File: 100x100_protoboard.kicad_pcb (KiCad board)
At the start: 2 copper layers, 97.8 x 96.5 mm, 418 parts, among them CON1 BARREL_JACK, CON2 USB_FEMALE_WITH_ID, CON3 USB_FEMALE_WITH_ID, J1 INTERCONNECT_1X03, J10 INTERCONNECT_1X03, J11 INTERCONNECT_1X03, J12 INTERCONNECT_1X03, J13 INTERCONNECT_1X03, J14 INTERCONNECT_1X03, J15 INTERCONNECT_1X03, J16 INTERCONNECT_1X03, J17 INTERCONNECT_1X03, J18 INTERCONNECT_1X03, J19 INTERCONNECT_1X03, J2 INTERCONNECT_1X03, J20 INTERCONNECT_1X03, J21 INTERCONNECT_1X03, J22 INTERCONNECT_1X03, J23 INTERCONNECT_1X03, J24 INTERCONNECT_1X03, J25 INTERCONNECT_1X03, J26 INTERCONNECT_1X03, J27 INTERCONNECT_1X03, J28 INTERCONNECT_1X03, J29 INTERCONNECT_1X03, J3 INTERCONNECT_1X03, J30 INTERCONNECT_1X03, J31 INTERCONNECT_1X03, J32 INTERCONNECT_1X03, J33 INTERCONNECT_1X03, J34 INTERCONNECT_1X03, J35 INTERCONNECT_1X03, J36 INTERCONNECT_1X03, J37 INTERCONNECT_1X03, J38 INTERCONNECT_1X03, J39 INTERCONNECT_1X03, J4 INTERCONNECT_1X03, J40 INTERCONNECT_1X03, J41 INTERCONNECT_1X03, J42 INTERCONNECT_1X03, J43 INTERCONNECT_1X03, J44 INTERCONNECT_1X03, J45 INTERCONNECT_1X03, J46 INTERCONNECT_1X03, J47 INTERCONNECT_1X03, J48 INTERCONNECT_1X03, J49 INTERCONNECT_1X03, J5 INTERCONNECT_1X03, J50 INTERCONNECT_1X03, J51 INTERCONNECT_1X03, J52 INTERCONNECT_1X03, J53 INTERCONNECT_1X03, J54 INTERCONNECT_1X03, J55 INTERCONNECT_1X03, J56 INTERCONNECT_1X03, J57 INTERCONNECT_1X03, J58 INTERCONNECT_1X03, J59 INTERCONNECT_1X03, J6 INTERCONNECT_1X03, J60 INTERCONNECT_1X03, J61 INTERCONNECT_1X03, J62 INTERCONNECT_1X03, J63 INTERCONNECT_1X03, J64 INTERCONNECT_1X03, J65 INTERCONNECT_1X02, J7 INTERCONNECT_1X03, J8 INTERCONNECT_1X03, J9 INTERCONNECT_1X03, P1 CONN_5, P1 CONN_8X2, P2 CONN_8X2, U1 LM7805CT

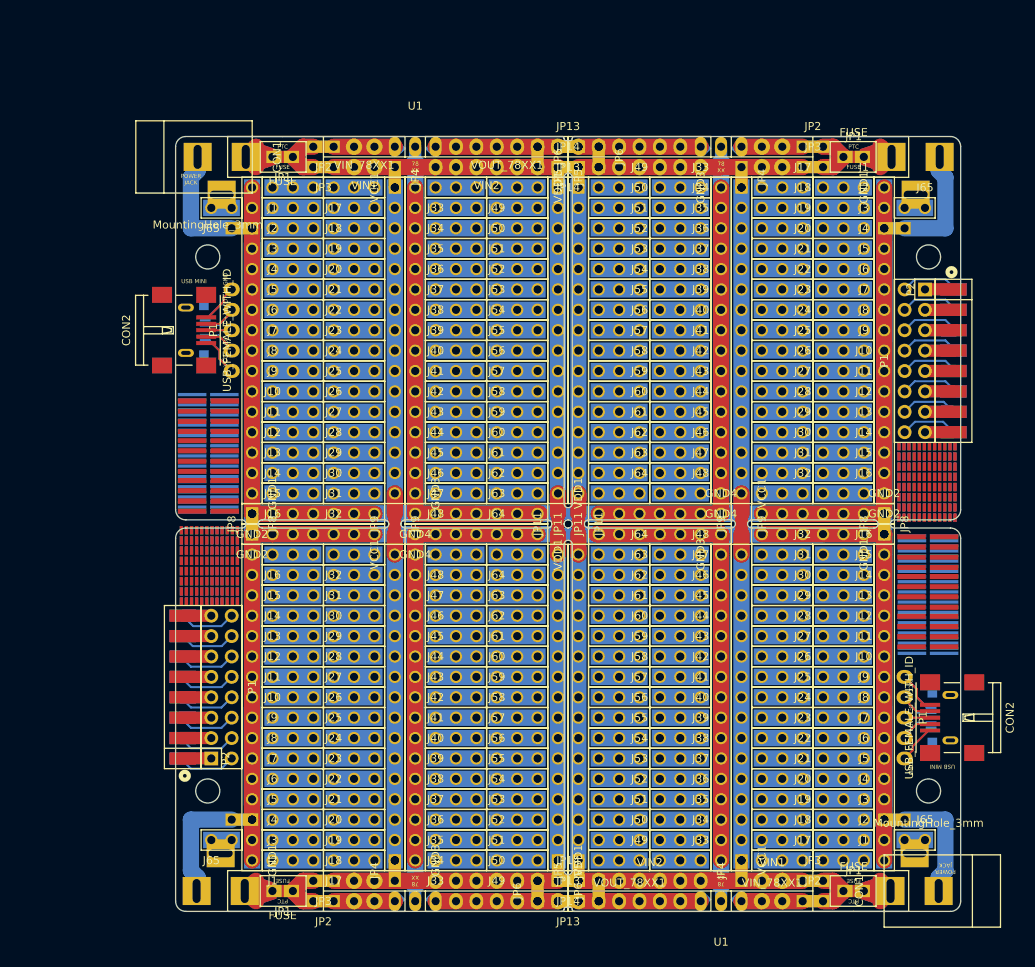
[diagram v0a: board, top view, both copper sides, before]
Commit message: remove center border outline, because drilling it plated shorts PWR and GND
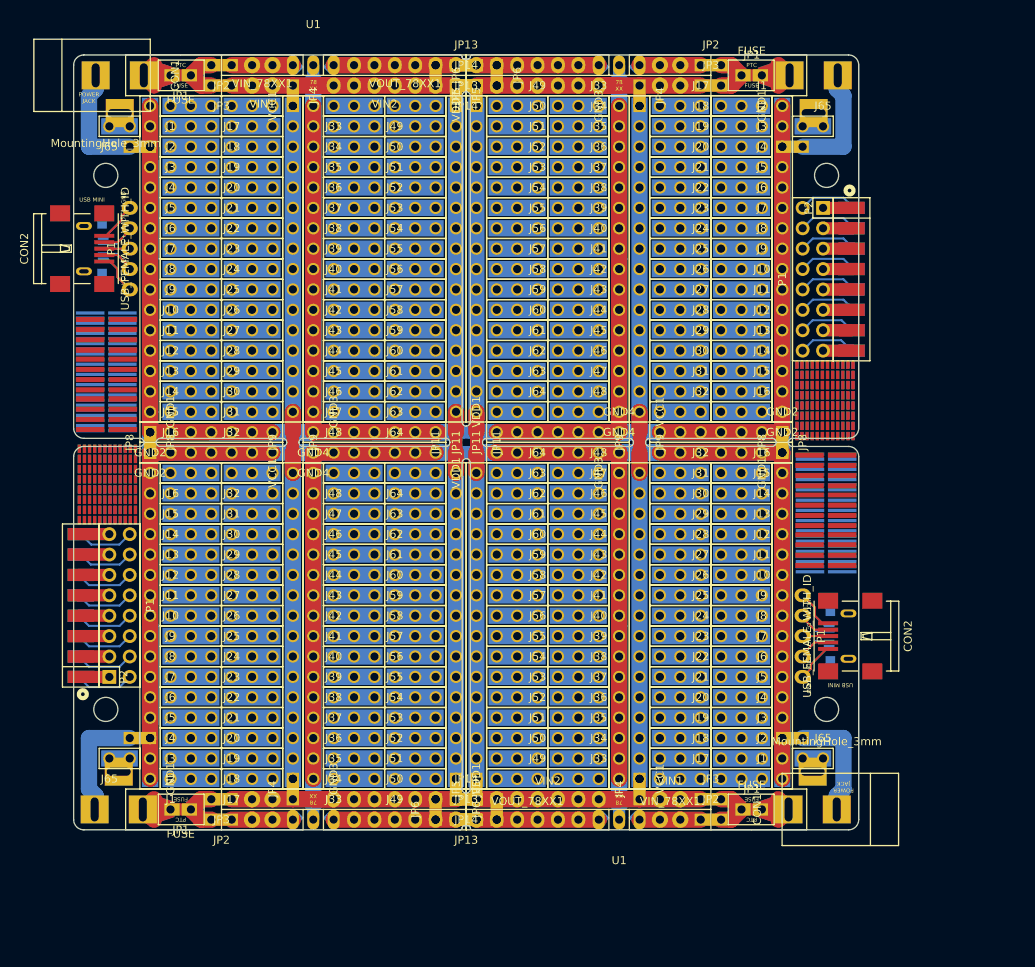
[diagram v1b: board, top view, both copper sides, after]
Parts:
- removed the C1 at (106.7, 35.3)
- removed the C1 at (106.7, 127.3)
- removed the C2 at (104.1, 35.3)
- removed the C2 at (104.1, 127.3)
- removed the CON1 at (132.8, 35.6)
- removed the CON1 at (132.7, 127.0)
- removed the F1 at (121.9, 35.6)
- removed the F1 at (121.9, 127.0)
- removed the F2 at (121.9, 35.6)
- removed the F2 at (121.9, 127.0)
- removed the GND1 at (125.7, 39.4)
- removed the GND1 at (125.7, 85.1)
- removed the GND2 at (125.7, 80.0)
- removed the GND2 at (125.7, 82.5)
- removed the GND3 at (105.4, 39.4)
- removed the GND3 at (105.4, 85.1)
- removed the GND4 at (105.4, 80.0)
- removed the GND4 at (105.4, 82.5)
- removed the J1 at (123.2, 39.4)
- removed the J1 at (123.2, 123.2)
- removed the J10 at (123.2, 62.2)
- removed the J10 at (123.2, 100.3)
- removed the J11 at (123.2, 64.8)
- removed the J11 at (123.2, 97.8)
- removed the J12 at (123.2, 67.3)
- removed the J12 at (123.2, 95.2)
- removed the J13 at (123.2, 69.8)
- removed the J13 at (123.2, 92.7)
- removed the J14 at (123.2, 72.4)
- removed the J14 at (123.2, 90.2)
- removed the J15 at (123.2, 74.9)
- removed the J15 at (123.2, 87.6)
- removed the J16 at (123.2, 77.5)
- removed the J16 at (123.2, 85.1)
- removed the J17 at (115.6, 39.4)
- removed the J17 at (115.6, 123.2)
- removed the J18 at (115.6, 41.9)
- removed the J18 at (115.6, 120.7)
- removed the J19 at (115.6, 44.5)
- removed the J19 at (115.6, 118.1)
- removed the J2 at (123.2, 41.9)
- removed the J2 at (123.2, 120.7)
- removed the J20 at (115.6, 47.0)
- removed the J20 at (115.6, 115.6)
- removed the J21 at (115.6, 49.5)
- removed the J21 at (115.6, 113.0)
- removed the J22 at (115.6, 52.1)
- removed the J22 at (115.6, 110.5)
- removed the J23 at (115.6, 54.6)
- removed the J23 at (115.6, 108.0)
- removed the J24 at (115.6, 57.1)
- removed the J24 at (115.6, 105.4)
- removed the J25 at (115.6, 59.7)
- removed the J25 at (115.6, 102.9)
- removed the J26 at (115.6, 62.2)
- removed the J26 at (115.6, 100.3)
- removed the J27 at (115.6, 64.8)
- removed the J27 at (115.6, 97.8)
- removed the J28 at (115.6, 67.3)
- removed the J28 at (115.6, 95.2)
- removed the J29 at (115.6, 69.8)
- removed the J29 at (115.6, 92.7)
- removed the J3 at (123.2, 44.5)
- removed the J3 at (123.2, 118.1)
- removed the J30 at (115.6, 72.4)
- removed the J30 at (115.6, 90.2)
- removed the J31 at (115.6, 74.9)
- removed the J31 at (115.6, 87.6)
- removed the J32 at (115.6, 77.5)
- removed the J32 at (115.6, 85.1)
- removed the J33 at (102.9, 39.4)
- removed the J33 at (102.9, 123.2)
- removed the J34 at (102.9, 41.9)
- removed the J34 at (102.9, 120.7)
- removed the J35 at (102.9, 44.5)
- removed the J35 at (102.9, 118.1)
- removed the J36 at (102.9, 47.0)
- removed the J36 at (102.9, 115.6)
- removed the J37 at (102.9, 49.5)
- removed the J37 at (102.9, 113.0)
- removed the J38 at (102.9, 52.1)
- removed the J38 at (102.9, 110.5)
- removed the J39 at (102.9, 54.6)
- removed the J39 at (102.9, 108.0)
- removed the J4 at (123.2, 47.0)
- removed the J4 at (123.2, 115.6)
- removed the J40 at (102.9, 57.1)
- removed the J40 at (102.9, 105.4)
- removed the J41 at (102.9, 59.7)
- removed the J41 at (102.9, 102.9)
- removed the J42 at (102.9, 62.2)
- removed the J42 at (102.9, 100.3)
- removed the J43 at (102.9, 64.8)
- removed the J43 at (102.9, 97.8)
- removed the J44 at (102.9, 67.3)
- removed the J44 at (102.9, 95.2)
- removed the J45 at (102.9, 69.8)
- removed the J45 at (102.9, 92.7)
- removed the J46 at (102.9, 72.4)
- removed the J46 at (102.9, 90.2)
- removed the J47 at (102.9, 74.9)
- removed the J47 at (102.9, 87.6)
- removed the J48 at (102.9, 77.5)
- removed the J48 at (102.9, 85.1)
- removed the J49 at (95.2, 39.4)
- removed the J49 at (95.2, 123.2)
- removed the J5 at (123.2, 49.5)
- removed the J5 at (123.2, 113.0)
- removed the J50 at (95.2, 41.9)
- removed the J50 at (95.2, 120.7)
- removed the J51 at (95.2, 44.5)
- removed the J51 at (95.2, 118.1)
- removed the J52 at (95.2, 47.0)
- removed the J52 at (95.2, 115.6)
- removed the J53 at (95.2, 49.5)
- removed the J53 at (95.2, 113.0)
- removed the J54 at (95.2, 52.1)
- removed the J54 at (95.2, 110.5)
- removed the J55 at (95.2, 54.6)
- removed the J55 at (95.2, 108.0)
- removed the J56 at (95.2, 57.1)
- removed the J56 at (95.2, 105.4)
- removed the J57 at (95.2, 59.7)
- removed the J57 at (95.2, 102.9)
- removed the J58 at (95.2, 62.2)
- removed the J58 at (95.2, 100.3)
- removed the J59 at (95.2, 64.8)
- removed the J59 at (95.2, 97.8)
- removed the J6 at (123.2, 52.1)
- removed the J6 at (123.2, 110.5)
- removed the J60 at (95.2, 67.3)
- removed the J60 at (95.2, 95.2)
- removed the J61 at (95.2, 69.8)
- removed the J61 at (95.2, 92.7)
- removed the J62 at (95.2, 72.4)
- removed the J62 at (95.2, 90.2)
- removed the J63 at (95.2, 74.9)
- removed the J63 at (95.2, 87.6)
- removed the J64 at (95.2, 77.5)
- removed the J64 at (95.2, 85.1)
- removed the J65 at (130.8, 41.9)
- removed the J65 at (130.8, 120.7)
- removed the J7 at (123.2, 54.6)
- removed the J7 at (123.2, 108.0)
- removed the J8 at (123.2, 57.1)
- removed the J8 at (123.2, 105.4)
- removed the J9 at (123.2, 59.7)
- removed the J9 at (123.2, 102.9)
- removed the JP1 at (121.9, 35.6)
- removed the JP1 at (121.9, 127.0)
- removed the JP10 at (87.6, 81.3) (x2)
- removed the JP11 at (87.6, 81.3) (x2)
- removed the JP12 at (86.4, 80.0)
- removed the JP12 at (86.4, 82.5)
- removed the JP13 at (86.4, 34.3)
- removed the JP13 at (86.4, 128.3)
- removed the JP14 at (86.4, 36.8)
- removed the JP14 at (86.4, 125.7)
- removed the JP15 at (108.0, 81.3) (x2)
- removed the JP2 at (116.8, 34.3)
- removed the JP2 at (116.8, 128.3)
- removed the JP3 at (116.8, 36.8)
- removed the JP3 at (116.8, 125.7)
- removed the JP4 at (108.0, 38.1)
- removed the JP4 at (108.0, 124.5)
- removed the JP5 at (87.6, 38.1)
- removed the JP5 at (87.6, 124.5)
- removed the JP6 at (90.2, 35.6)
- removed the JP6 at (90.2, 127.0)
- removed the JP7 at (127.0, 44.5)
- removed the JP7 at (127.0, 118.1)
- removed the JP8 at (125.7, 81.3) (x2)
- removed the JP9 at (108.0, 81.3) (x2)
- removed the MountingHole_3mm at (131.2, 48.0)
- removed the MountingHole_3mm at (131.2, 114.5)
- removed the P1 at (129.5, 61.0)
- removed the P1 at (128.3, 105.4)
- removed the Ref** at (131.7, 78.6) (x2)
- removed the Ref** at (131.2, 95.2)
- removed the Ref** at (131.7, 73.5) (x2)
- removed the Ref** at (131.2, 94.7)
- removed the Ref** at (131.2, 89.7)
- removed the Ref** at (131.2, 84.8)
- removed the Ref** at (131.2, 85.0)
- removed the Ref** at (131.2, 90.1)
- removed the U1 at (105.4, 34.3)
- removed the U1 at (105.4, 128.3)
- removed the VCC1 at (108.0, 77.5)
- removed the VCC1 at (108.0, 123.2)
- removed the VDD1 at (87.6, 39.4)
- removed the VDD1 at (87.6, 85.1)
- removed the VIN1 at (111.8, 36.8)
- removed the VIN1 at (111.8, 125.7)
- removed the VIN2 at (96.5, 36.8)
- removed the VIN2 at (96.5, 125.7)
- removed the VIN_78XX1 at (111.8, 34.3)
- removed the VIN_78XX1 at (111.8, 128.3)
- removed the VOUT_78XX1 at (94.0, 34.3)
- removed the VOUT_78XX1 at (94.0, 128.3)
- added C1: u33, Capacitors_SMD:C_0805_HandSoldering, B.Cu at (94.0, 25.1)
- added C1: u33, Capacitors_SMD:C_0805_HandSoldering, B.Cu at (94.0, 117.1)
- added C2: u1, Capacitors_SMD:C_0805_HandSoldering, B.Cu at (91.4, 25.1)
- added C2: u1, Capacitors_SMD:C_0805_HandSoldering, B.Cu at (91.4, 117.1)
- added CON1: BARREL_JACK, Connect:BARREL_JACK, B.Cu at (120.1, 25.4)
- added CON1: BARREL_JACK, Connect:BARREL_JACK, F.Cu at (120.0, 116.8)
- added F1: FUSE, Muonde:CC12ZZ, B.Cu at (109.2, 25.4)
- added F1: FUSE, Muonde:CC12ZZ, F.Cu at (109.2, 116.8)
- added F2: FUSE, Muonde:CC12ZZ, F.Cu at (109.2, 25.4)
- added F2: FUSE, Muonde:CC12ZZ, B.Cu at (109.2, 116.8)
- added GND1: INTERCONNECT_1X16, 2.54mm_Pin_Headers:Interconnect_1x16, F.Cu at (113.0, 29.2)
- added GND1: INTERCONNECT_1X16, 2.54mm_Pin_Headers:Interconnect_1x16, F.Cu at (113.0, 74.9)
- added GND2: INTERCONNECT_1X07, 2.54mm_Pin_Headers:Interconnect_1x07, F.Cu at (113.0, 69.8)
- added GND2: INTERCONNECT_1X07, 2.54mm_Pin_Headers:Interconnect_1x07, F.Cu at (113.0, 72.4)
- added GND3: INTERCONNECT_1X16, 2.54mm_Pin_Headers:Interconnect_1x16, F.Cu at (92.7, 29.2)
- added GND3: INTERCONNECT_1X16, 2.54mm_Pin_Headers:Interconnect_1x16, F.Cu at (92.7, 74.9)
- added GND4: INTERCONNECT_1X07, 2.54mm_Pin_Headers:Interconnect_1x07, F.Cu at (92.7, 69.8)
- added GND4: INTERCONNECT_1X07, 2.54mm_Pin_Headers:Interconnect_1x07, F.Cu at (92.7, 72.4)
- added J1: INTERCONNECT_1X03, 2.54mm_Pin_Headers:Interconnect_1x03, F.Cu at (110.5, 29.2)
- added J1: INTERCONNECT_1X03, 2.54mm_Pin_Headers:Interconnect_1x03, F.Cu at (110.5, 113.0)
- added J10: INTERCONNECT_1X03, 2.54mm_Pin_Headers:Interconnect_1x03, F.Cu at (110.5, 52.1)
- added J10: INTERCONNECT_1X03, 2.54mm_Pin_Headers:Interconnect_1x03, F.Cu at (110.5, 90.2)
- added J11: INTERCONNECT_1X03, 2.54mm_Pin_Headers:Interconnect_1x03, F.Cu at (110.5, 54.6)
- added J11: INTERCONNECT_1X03, 2.54mm_Pin_Headers:Interconnect_1x03, F.Cu at (110.5, 87.6)
- added J12: INTERCONNECT_1X03, 2.54mm_Pin_Headers:Interconnect_1x03, F.Cu at (110.5, 57.1)
- added J12: INTERCONNECT_1X03, 2.54mm_Pin_Headers:Interconnect_1x03, F.Cu at (110.5, 85.1)
- added J13: INTERCONNECT_1X03, 2.54mm_Pin_Headers:Interconnect_1x03, F.Cu at (110.5, 59.7)
- added J13: INTERCONNECT_1X03, 2.54mm_Pin_Headers:Interconnect_1x03, F.Cu at (110.5, 82.5)
- added J14: INTERCONNECT_1X03, 2.54mm_Pin_Headers:Interconnect_1x03, F.Cu at (110.5, 62.2)
- added J14: INTERCONNECT_1X03, 2.54mm_Pin_Headers:Interconnect_1x03, F.Cu at (110.5, 80.0)
- added J15: INTERCONNECT_1X03, 2.54mm_Pin_Headers:Interconnect_1x03, F.Cu at (110.5, 64.8)
- added J15: INTERCONNECT_1X03, 2.54mm_Pin_Headers:Interconnect_1x03, F.Cu at (110.5, 77.5)
- added J16: INTERCONNECT_1X03, 2.54mm_Pin_Headers:Interconnect_1x03, F.Cu at (110.5, 67.3)
- added J16: INTERCONNECT_1X03, 2.54mm_Pin_Headers:Interconnect_1x03, F.Cu at (110.5, 74.9)
- added J17: INTERCONNECT_1X03, 2.54mm_Pin_Headers:Interconnect_1x03, F.Cu at (102.9, 29.2)
- added J17: INTERCONNECT_1X03, 2.54mm_Pin_Headers:Interconnect_1x03, F.Cu at (102.9, 113.0)
- added J18: INTERCONNECT_1X03, 2.54mm_Pin_Headers:Interconnect_1x03, F.Cu at (102.9, 31.8)
- added J18: INTERCONNECT_1X03, 2.54mm_Pin_Headers:Interconnect_1x03, F.Cu at (102.9, 110.5)
- added J19: INTERCONNECT_1X03, 2.54mm_Pin_Headers:Interconnect_1x03, F.Cu at (102.9, 34.3)
- added J19: INTERCONNECT_1X03, 2.54mm_Pin_Headers:Interconnect_1x03, F.Cu at (102.9, 108.0)
- added J2: INTERCONNECT_1X03, 2.54mm_Pin_Headers:Interconnect_1x03, F.Cu at (110.5, 31.8)
- added J2: INTERCONNECT_1X03, 2.54mm_Pin_Headers:Interconnect_1x03, F.Cu at (110.5, 110.5)
- added J20: INTERCONNECT_1X03, 2.54mm_Pin_Headers:Interconnect_1x03, F.Cu at (102.9, 36.8)
- added J20: INTERCONNECT_1X03, 2.54mm_Pin_Headers:Interconnect_1x03, F.Cu at (102.9, 105.4)
- added J21: INTERCONNECT_1X03, 2.54mm_Pin_Headers:Interconnect_1x03, F.Cu at (102.9, 39.4)
- added J21: INTERCONNECT_1X03, 2.54mm_Pin_Headers:Interconnect_1x03, F.Cu at (102.9, 102.9)
- added J22: INTERCONNECT_1X03, 2.54mm_Pin_Headers:Interconnect_1x03, F.Cu at (102.9, 41.9)
- added J22: INTERCONNECT_1X03, 2.54mm_Pin_Headers:Interconnect_1x03, F.Cu at (102.9, 100.3)
- added J23: INTERCONNECT_1X03, 2.54mm_Pin_Headers:Interconnect_1x03, F.Cu at (102.9, 44.5)
- added J23: INTERCONNECT_1X03, 2.54mm_Pin_Headers:Interconnect_1x03, F.Cu at (102.9, 97.8)
- added J24: INTERCONNECT_1X03, 2.54mm_Pin_Headers:Interconnect_1x03, F.Cu at (102.9, 47.0)
- added J24: INTERCONNECT_1X03, 2.54mm_Pin_Headers:Interconnect_1x03, F.Cu at (102.9, 95.2)
- added J25: INTERCONNECT_1X03, 2.54mm_Pin_Headers:Interconnect_1x03, F.Cu at (102.9, 49.5)
- added J25: INTERCONNECT_1X03, 2.54mm_Pin_Headers:Interconnect_1x03, F.Cu at (102.9, 92.7)
- added J26: INTERCONNECT_1X03, 2.54mm_Pin_Headers:Interconnect_1x03, F.Cu at (102.9, 52.1)
- added J26: INTERCONNECT_1X03, 2.54mm_Pin_Headers:Interconnect_1x03, F.Cu at (102.9, 90.2)
- added J27: INTERCONNECT_1X03, 2.54mm_Pin_Headers:Interconnect_1x03, F.Cu at (102.9, 54.6)
- added J27: INTERCONNECT_1X03, 2.54mm_Pin_Headers:Interconnect_1x03, F.Cu at (102.9, 87.6)
- added J28: INTERCONNECT_1X03, 2.54mm_Pin_Headers:Interconnect_1x03, F.Cu at (102.9, 57.1)
- added J28: INTERCONNECT_1X03, 2.54mm_Pin_Headers:Interconnect_1x03, F.Cu at (102.9, 85.1)
- added J29: INTERCONNECT_1X03, 2.54mm_Pin_Headers:Interconnect_1x03, F.Cu at (102.9, 59.7)
- added J29: INTERCONNECT_1X03, 2.54mm_Pin_Headers:Interconnect_1x03, F.Cu at (102.9, 82.5)
- added J3: INTERCONNECT_1X03, 2.54mm_Pin_Headers:Interconnect_1x03, F.Cu at (110.5, 34.3)
- added J3: INTERCONNECT_1X03, 2.54mm_Pin_Headers:Interconnect_1x03, F.Cu at (110.5, 108.0)
- added J30: INTERCONNECT_1X03, 2.54mm_Pin_Headers:Interconnect_1x03, F.Cu at (102.9, 62.2)
- added J30: INTERCONNECT_1X03, 2.54mm_Pin_Headers:Interconnect_1x03, F.Cu at (102.9, 80.0)
- added J31: INTERCONNECT_1X03, 2.54mm_Pin_Headers:Interconnect_1x03, F.Cu at (102.9, 64.8)
- added J31: INTERCONNECT_1X03, 2.54mm_Pin_Headers:Interconnect_1x03, F.Cu at (102.9, 77.5)
- added J32: INTERCONNECT_1X03, 2.54mm_Pin_Headers:Interconnect_1x03, F.Cu at (102.9, 67.3)
- added J32: INTERCONNECT_1X03, 2.54mm_Pin_Headers:Interconnect_1x03, F.Cu at (102.9, 74.9)
- added J33: INTERCONNECT_1X03, 2.54mm_Pin_Headers:Interconnect_1x03, F.Cu at (90.2, 29.2)
- added J33: INTERCONNECT_1X03, 2.54mm_Pin_Headers:Interconnect_1x03, F.Cu at (90.2, 113.0)
- added J34: INTERCONNECT_1X03, 2.54mm_Pin_Headers:Interconnect_1x03, F.Cu at (90.2, 31.8)
- added J34: INTERCONNECT_1X03, 2.54mm_Pin_Headers:Interconnect_1x03, F.Cu at (90.2, 110.5)
- added J35: INTERCONNECT_1X03, 2.54mm_Pin_Headers:Interconnect_1x03, F.Cu at (90.2, 34.3)
- added J35: INTERCONNECT_1X03, 2.54mm_Pin_Headers:Interconnect_1x03, F.Cu at (90.2, 108.0)
- added J36: INTERCONNECT_1X03, 2.54mm_Pin_Headers:Interconnect_1x03, F.Cu at (90.2, 36.8)
- added J36: INTERCONNECT_1X03, 2.54mm_Pin_Headers:Interconnect_1x03, F.Cu at (90.2, 105.4)
- added J37: INTERCONNECT_1X03, 2.54mm_Pin_Headers:Interconnect_1x03, F.Cu at (90.2, 39.4)
- added J37: INTERCONNECT_1X03, 2.54mm_Pin_Headers:Interconnect_1x03, F.Cu at (90.2, 102.9)
- added J38: INTERCONNECT_1X03, 2.54mm_Pin_Headers:Interconnect_1x03, F.Cu at (90.2, 41.9)
- added J38: INTERCONNECT_1X03, 2.54mm_Pin_Headers:Interconnect_1x03, F.Cu at (90.2, 100.3)
- added J39: INTERCONNECT_1X03, 2.54mm_Pin_Headers:Interconnect_1x03, F.Cu at (90.2, 44.5)
- added J39: INTERCONNECT_1X03, 2.54mm_Pin_Headers:Interconnect_1x03, F.Cu at (90.2, 97.8)
- added J4: INTERCONNECT_1X03, 2.54mm_Pin_Headers:Interconnect_1x03, F.Cu at (110.5, 36.8)
- added J4: INTERCONNECT_1X03, 2.54mm_Pin_Headers:Interconnect_1x03, F.Cu at (110.5, 105.4)
- added J40: INTERCONNECT_1X03, 2.54mm_Pin_Headers:Interconnect_1x03, F.Cu at (90.2, 47.0)
- added J40: INTERCONNECT_1X03, 2.54mm_Pin_Headers:Interconnect_1x03, F.Cu at (90.2, 95.2)
- added J41: INTERCONNECT_1X03, 2.54mm_Pin_Headers:Interconnect_1x03, F.Cu at (90.2, 49.5)
- added J41: INTERCONNECT_1X03, 2.54mm_Pin_Headers:Interconnect_1x03, F.Cu at (90.2, 92.7)
- added J42: INTERCONNECT_1X03, 2.54mm_Pin_Headers:Interconnect_1x03, F.Cu at (90.2, 52.1)
- added J42: INTERCONNECT_1X03, 2.54mm_Pin_Headers:Interconnect_1x03, F.Cu at (90.2, 90.2)
- added J43: INTERCONNECT_1X03, 2.54mm_Pin_Headers:Interconnect_1x03, F.Cu at (90.2, 54.6)
- added J43: INTERCONNECT_1X03, 2.54mm_Pin_Headers:Interconnect_1x03, F.Cu at (90.2, 87.6)
- added J44: INTERCONNECT_1X03, 2.54mm_Pin_Headers:Interconnect_1x03, F.Cu at (90.2, 57.1)
- added J44: INTERCONNECT_1X03, 2.54mm_Pin_Headers:Interconnect_1x03, F.Cu at (90.2, 85.1)
- added J45: INTERCONNECT_1X03, 2.54mm_Pin_Headers:Interconnect_1x03, F.Cu at (90.2, 59.7)
- added J45: INTERCONNECT_1X03, 2.54mm_Pin_Headers:Interconnect_1x03, F.Cu at (90.2, 82.5)
- added J46: INTERCONNECT_1X03, 2.54mm_Pin_Headers:Interconnect_1x03, F.Cu at (90.2, 62.2)
- added J46: INTERCONNECT_1X03, 2.54mm_Pin_Headers:Interconnect_1x03, F.Cu at (90.2, 80.0)
- added J47: INTERCONNECT_1X03, 2.54mm_Pin_Headers:Interconnect_1x03, F.Cu at (90.2, 64.8)
- added J47: INTERCONNECT_1X03, 2.54mm_Pin_Headers:Interconnect_1x03, F.Cu at (90.2, 77.5)
- added J48: INTERCONNECT_1X03, 2.54mm_Pin_Headers:Interconnect_1x03, F.Cu at (90.2, 67.3)
- added J48: INTERCONNECT_1X03, 2.54mm_Pin_Headers:Interconnect_1x03, F.Cu at (90.2, 74.9)
- added J49: INTERCONNECT_1X03, 2.54mm_Pin_Headers:Interconnect_1x03, F.Cu at (82.5, 29.2)
- added J49: INTERCONNECT_1X03, 2.54mm_Pin_Headers:Interconnect_1x03, F.Cu at (82.5, 113.0)
- added J5: INTERCONNECT_1X03, 2.54mm_Pin_Headers:Interconnect_1x03, F.Cu at (110.5, 39.4)
- added J5: INTERCONNECT_1X03, 2.54mm_Pin_Headers:Interconnect_1x03, F.Cu at (110.5, 102.9)
- added J50: INTERCONNECT_1X03, 2.54mm_Pin_Headers:Interconnect_1x03, F.Cu at (82.5, 31.8)
- added J50: INTERCONNECT_1X03, 2.54mm_Pin_Headers:Interconnect_1x03, F.Cu at (82.5, 110.5)
- added J51: INTERCONNECT_1X03, 2.54mm_Pin_Headers:Interconnect_1x03, F.Cu at (82.5, 34.3)
- added J51: INTERCONNECT_1X03, 2.54mm_Pin_Headers:Interconnect_1x03, F.Cu at (82.5, 108.0)
- added J52: INTERCONNECT_1X03, 2.54mm_Pin_Headers:Interconnect_1x03, F.Cu at (82.5, 36.8)
- added J52: INTERCONNECT_1X03, 2.54mm_Pin_Headers:Interconnect_1x03, F.Cu at (82.5, 105.4)
- added J53: INTERCONNECT_1X03, 2.54mm_Pin_Headers:Interconnect_1x03, F.Cu at (82.5, 39.4)
- added J53: INTERCONNECT_1X03, 2.54mm_Pin_Headers:Interconnect_1x03, F.Cu at (82.5, 102.9)
- added J54: INTERCONNECT_1X03, 2.54mm_Pin_Headers:Interconnect_1x03, F.Cu at (82.5, 41.9)
- added J54: INTERCONNECT_1X03, 2.54mm_Pin_Headers:Interconnect_1x03, F.Cu at (82.5, 100.3)
- added J55: INTERCONNECT_1X03, 2.54mm_Pin_Headers:Interconnect_1x03, F.Cu at (82.5, 44.5)
- added J55: INTERCONNECT_1X03, 2.54mm_Pin_Headers:Interconnect_1x03, F.Cu at (82.5, 97.8)
- added J56: INTERCONNECT_1X03, 2.54mm_Pin_Headers:Interconnect_1x03, F.Cu at (82.5, 47.0)
- added J56: INTERCONNECT_1X03, 2.54mm_Pin_Headers:Interconnect_1x03, F.Cu at (82.5, 95.2)
- added J57: INTERCONNECT_1X03, 2.54mm_Pin_Headers:Interconnect_1x03, F.Cu at (82.5, 49.5)
- added J57: INTERCONNECT_1X03, 2.54mm_Pin_Headers:Interconnect_1x03, F.Cu at (82.5, 92.7)
- added J58: INTERCONNECT_1X03, 2.54mm_Pin_Headers:Interconnect_1x03, F.Cu at (82.5, 52.1)
- added J58: INTERCONNECT_1X03, 2.54mm_Pin_Headers:Interconnect_1x03, F.Cu at (82.5, 90.2)
- added J59: INTERCONNECT_1X03, 2.54mm_Pin_Headers:Interconnect_1x03, F.Cu at (82.5, 54.6)
- added J59: INTERCONNECT_1X03, 2.54mm_Pin_Headers:Interconnect_1x03, F.Cu at (82.5, 87.6)
- added J6: INTERCONNECT_1X03, 2.54mm_Pin_Headers:Interconnect_1x03, F.Cu at (110.5, 41.9)
- added J6: INTERCONNECT_1X03, 2.54mm_Pin_Headers:Interconnect_1x03, F.Cu at (110.5, 100.3)
- added J60: INTERCONNECT_1X03, 2.54mm_Pin_Headers:Interconnect_1x03, F.Cu at (82.5, 57.1)
- added J60: INTERCONNECT_1X03, 2.54mm_Pin_Headers:Interconnect_1x03, F.Cu at (82.5, 85.1)
- added J61: INTERCONNECT_1X03, 2.54mm_Pin_Headers:Interconnect_1x03, F.Cu at (82.5, 59.7)
- added J61: INTERCONNECT_1X03, 2.54mm_Pin_Headers:Interconnect_1x03, F.Cu at (82.5, 82.5)
- added J62: INTERCONNECT_1X03, 2.54mm_Pin_Headers:Interconnect_1x03, F.Cu at (82.5, 62.2)
- added J62: INTERCONNECT_1X03, 2.54mm_Pin_Headers:Interconnect_1x03, F.Cu at (82.5, 80.0)
- added J63: INTERCONNECT_1X03, 2.54mm_Pin_Headers:Interconnect_1x03, F.Cu at (82.5, 64.8)
- added J63: INTERCONNECT_1X03, 2.54mm_Pin_Headers:Interconnect_1x03, F.Cu at (82.5, 77.5)
- added J64: INTERCONNECT_1X03, 2.54mm_Pin_Headers:Interconnect_1x03, F.Cu at (82.5, 67.3)
- added J64: INTERCONNECT_1X03, 2.54mm_Pin_Headers:Interconnect_1x03, F.Cu at (82.5, 74.9)
- added J65: INTERCONNECT_1X02, 2.54mm_Pin_Headers:Interconnect_1x02, F.Cu at (118.1, 31.8)
- added J65: INTERCONNECT_1X02, 2.54mm_Pin_Headers:Interconnect_1x02, F.Cu at (118.1, 110.5)
- added J7: INTERCONNECT_1X03, 2.54mm_Pin_Headers:Interconnect_1x03, F.Cu at (110.5, 44.5)
- added J7: INTERCONNECT_1X03, 2.54mm_Pin_Headers:Interconnect_1x03, F.Cu at (110.5, 97.8)
- added J8: INTERCONNECT_1X03, 2.54mm_Pin_Headers:Interconnect_1x03, F.Cu at (110.5, 47.0)
- added J8: INTERCONNECT_1X03, 2.54mm_Pin_Headers:Interconnect_1x03, F.Cu at (110.5, 95.2)
- added J9: INTERCONNECT_1X03, 2.54mm_Pin_Headers:Interconnect_1x03, F.Cu at (110.5, 49.5)
- added J9: INTERCONNECT_1X03, 2.54mm_Pin_Headers:Interconnect_1x03, F.Cu at (110.5, 92.7)
- added JP1: JUMPER, 2.54mm_Pin_Headers:Solder_Jumper_1x2_Shorted_T, F.Cu at (109.2, 25.4)
- added JP1: JUMPER, 2.54mm_Pin_Headers:Solder_Jumper_1x2_Shorted_T, F.Cu at (109.2, 116.8)
- added JP10 (x2): JUMPER, 2.54mm_Pin_Headers:Solder_Jumper_SMD_1x2_Shorted, B.Cu at (74.9, 71.1)
- added JP11 (x2): JUMPER, 2.54mm_Pin_Headers:Solder_Jumper_SMD_1x2_Shorted, F.Cu at (74.9, 71.1)
- added JP12: JUMPER, 2.54mm_Pin_Headers:Solder_Jumper_SMD_1x2_Shorted, B.Cu at (73.7, 69.8)
- added JP12: JUMPER, 2.54mm_Pin_Headers:Solder_Jumper_SMD_1x2_Shorted, B.Cu at (73.7, 72.4)
- added JP13: JUMPER, 2.54mm_Pin_Headers:Solder_Jumper_1x2_Shorted_T, F.Cu at (73.7, 24.1)
- added JP13: JUMPER, 2.54mm_Pin_Headers:Solder_Jumper_1x2_Shorted_T, F.Cu at (73.7, 118.1)
- added JP14: JUMPER, 2.54mm_Pin_Headers:Solder_Jumper_1x2_Shorted_T, F.Cu at (73.7, 26.7)
- added JP14: JUMPER, 2.54mm_Pin_Headers:Solder_Jumper_1x2_Shorted_T, F.Cu at (73.7, 115.6)
- added JP15 (x2): JUMPER, 2.54mm_Pin_Headers:Solder_Jumper_SMD_1x2, B.Cu at (95.2, 71.1)
- added JP2: JUMPER, 2.54mm_Pin_Headers:Solder_Jumper_1x2_Shorted_T, F.Cu at (104.1, 24.1)
- added JP2: JUMPER, 2.54mm_Pin_Headers:Solder_Jumper_1x2_Shorted_T, F.Cu at (104.1, 118.1)
- added JP3: JUMPER, 2.54mm_Pin_Headers:Solder_Jumper_1x2_Shorted_T, F.Cu at (104.1, 26.7)
- added JP3: JUMPER, 2.54mm_Pin_Headers:Solder_Jumper_1x2_Shorted_T, F.Cu at (104.1, 115.6)
- added JP4: JUMPER, 2.54mm_Pin_Headers:Solder_Jumper_1x2_Shorted_T, F.Cu at (95.2, 27.9)
- added JP4: JUMPER, 2.54mm_Pin_Headers:Solder_Jumper_1x2_Shorted_T, F.Cu at (95.2, 114.3)
- added JP5: JUMPER, 2.54mm_Pin_Headers:Solder_Jumper_1x2_Shorted_T, F.Cu at (74.9, 27.9)
- added JP5: JUMPER, 2.54mm_Pin_Headers:Solder_Jumper_1x2_Shorted_T, F.Cu at (74.9, 114.3)
- added JP6: JUMPER, 2.54mm_Pin_Headers:Solder_Jumper_1x2_Shorted_T, F.Cu at (77.5, 25.4)
- added JP6: JUMPER, 2.54mm_Pin_Headers:Solder_Jumper_1x2_Shorted_T, F.Cu at (77.5, 116.8)
- added JP7: JUMPER, 2.54mm_Pin_Headers:Solder_Jumper_1x2_Shorted_T, B.Cu at (114.3, 34.3)
- added JP7: JUMPER, 2.54mm_Pin_Headers:Solder_Jumper_1x2_Shorted_T, B.Cu at (114.3, 108.0)
- added JP8 (x2): JUMPER, 2.54mm_Pin_Headers:Solder_Jumper_1x2, F.Cu at (113.0, 71.1)
- added JP9 (x2): JUMPER, 2.54mm_Pin_Headers:Solder_Jumper_SMD_1x2_Shorted, F.Cu at (95.2, 71.1)
- added MountingHole_3mm: VAL**, Mounting_Holes:MountingHole_3mm, B.Cu at (118.5, 37.9)
- added MountingHole_3mm: VAL**, Mounting_Holes:MountingHole_3mm, F.Cu at (118.5, 104.4)
- added P1: CONN_8X2, Socket_Strips:Socket_Strip_Straight_2x08, F.Cu at (116.8, 50.8)
- added P1: CONN_5, Socket_Strips:Socket_Strip_Straight_1x05, F.Cu at (115.6, 95.2)
- added Ref**: Val**, SMD:SMD_127_065_grid_4X12, F.Cu at (119.0, 68.4)
- added Ref**: Val**, SMD:SMD_065_357_8X2, B.Cu at (118.5, 85.0)
- added Ref**: Val**, SMD:SMD_127_065_grid_4X12, F.Cu at (119.0, 63.3)
- added Ref**: Val**, SMD:SMD_127_065_grid_4X12, B.Cu at (119.0, 68.4)
- added Ref**: Val**, SMD:SMD_127_065_grid_4X12, B.Cu at (119.0, 63.3)
- added Ref**: Val**, SMD:SMD_127_357_4X2, F.Cu at (118.5, 84.5)
- added Ref**: Val**, SMD:SMD_127_357_4X2, F.Cu at (118.5, 79.6)
- added Ref**: Val**, SMD:SMD_127_357_4X2, F.Cu at (118.5, 74.6)
- added Ref**: Val**, SMD:SMD_065_357_8X2, B.Cu at (118.5, 74.8)
- added Ref**: Val**, SMD:SMD_065_357_8X2, B.Cu at (118.5, 79.9)
- added U1: LM7805CT, Transistors_TO-220:TO-220_Neutral123_Vertical, B.Cu at (92.7, 24.1)
- added U1: LM7805CT, Transistors_TO-220:TO-220_Neutral123_Vertical, F.Cu at (92.7, 118.1)
- added VCC1: INTERCONNECT_1X16, 2.54mm_Pin_Headers:Interconnect_1x16, F.Cu at (95.2, 67.3)
- added VCC1: INTERCONNECT_1X16, 2.54mm_Pin_Headers:Interconnect_1x16, F.Cu at (95.2, 113.0)
- added VDD1: INTERCONNECT_1X16, 2.54mm_Pin_Headers:Interconnect_1x16, F.Cu at (74.9, 29.2)
- added VDD1: INTERCONNECT_1X16, 2.54mm_Pin_Headers:Interconnect_1x16, F.Cu at (74.9, 74.9)
- added VIN1: CONN_2, Socket_Strips:Socket_Strip_Straight_1x02, B.Cu at (99.1, 26.7)
- added VIN1: CONN_2, Socket_Strips:Socket_Strip_Straight_1x02, F.Cu at (99.1, 115.6)
- added VIN2: CONN_6, Socket_Strips:Socket_Strip_Straight_1x06, B.Cu at (83.8, 26.7)
- added VIN2: CONN_6, Socket_Strips:Socket_Strip_Straight_1x06, F.Cu at (83.8, 115.6)
- added VIN_78XX1: CONN_2, Socket_Strips:Socket_Strip_Straight_1x02, B.Cu at (99.1, 24.1)
- added VIN_78XX1: CONN_2, Socket_Strips:Socket_Strip_Straight_1x02, F.Cu at (99.1, 118.1)
- added VOUT_78XX1: CONN_6, Socket_Strips:Socket_Strip_Straight_1x06, B.Cu at (81.3, 24.1)
- added VOUT_78XX1: CONN_6, Socket_Strips:Socket_Strip_Straight_1x06, F.Cu at (81.3, 118.1)
- moved P2 16.3 mm to (121.7, 41.9)
- moved C1 16.3 mm to (53.3, 117.1)
- moved GND2 16.3 mm to (34.3, 69.8)
- moved GND4 16.3 mm to (54.6, 69.8)
- moved J11 16.3 mm to (36.8, 87.6)
- moved J15 16.3 mm to (36.8, 64.8)
- moved J2 16.3 mm to (36.8, 110.5)
- moved J50 16.3 mm to (64.8, 110.5)
- moved J57 16.3 mm to (64.8, 92.7)
- moved J59 16.3 mm to (64.8, 87.6)
- moved J63 16.3 mm to (64.8, 64.8)
- moved J9 16.3 mm to (36.8, 92.7)
- moved JP12 16.3 mm to (73.7, 69.8)
- moved JP13 16.3 mm to (73.7, 118.1)
- moved JP14 16.3 mm to (73.7, 115.6)
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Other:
- outline, holes or cut-outs redrawn
